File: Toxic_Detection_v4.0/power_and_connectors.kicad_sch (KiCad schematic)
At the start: 50 parts, among them IC7 ESDA6V1U1RL, IC8 AP7365-33WG-7, IC9 TPS2054BDR, J10 USB_C_Receptacle, J11 DM3AT-SF-PEJM5, J12 Conn_01x04_Pin, J13 Conn_ARM_JTAG_SWD_20, J8 Conn_01x04_Pin, J9 Conn_01x04_Pin

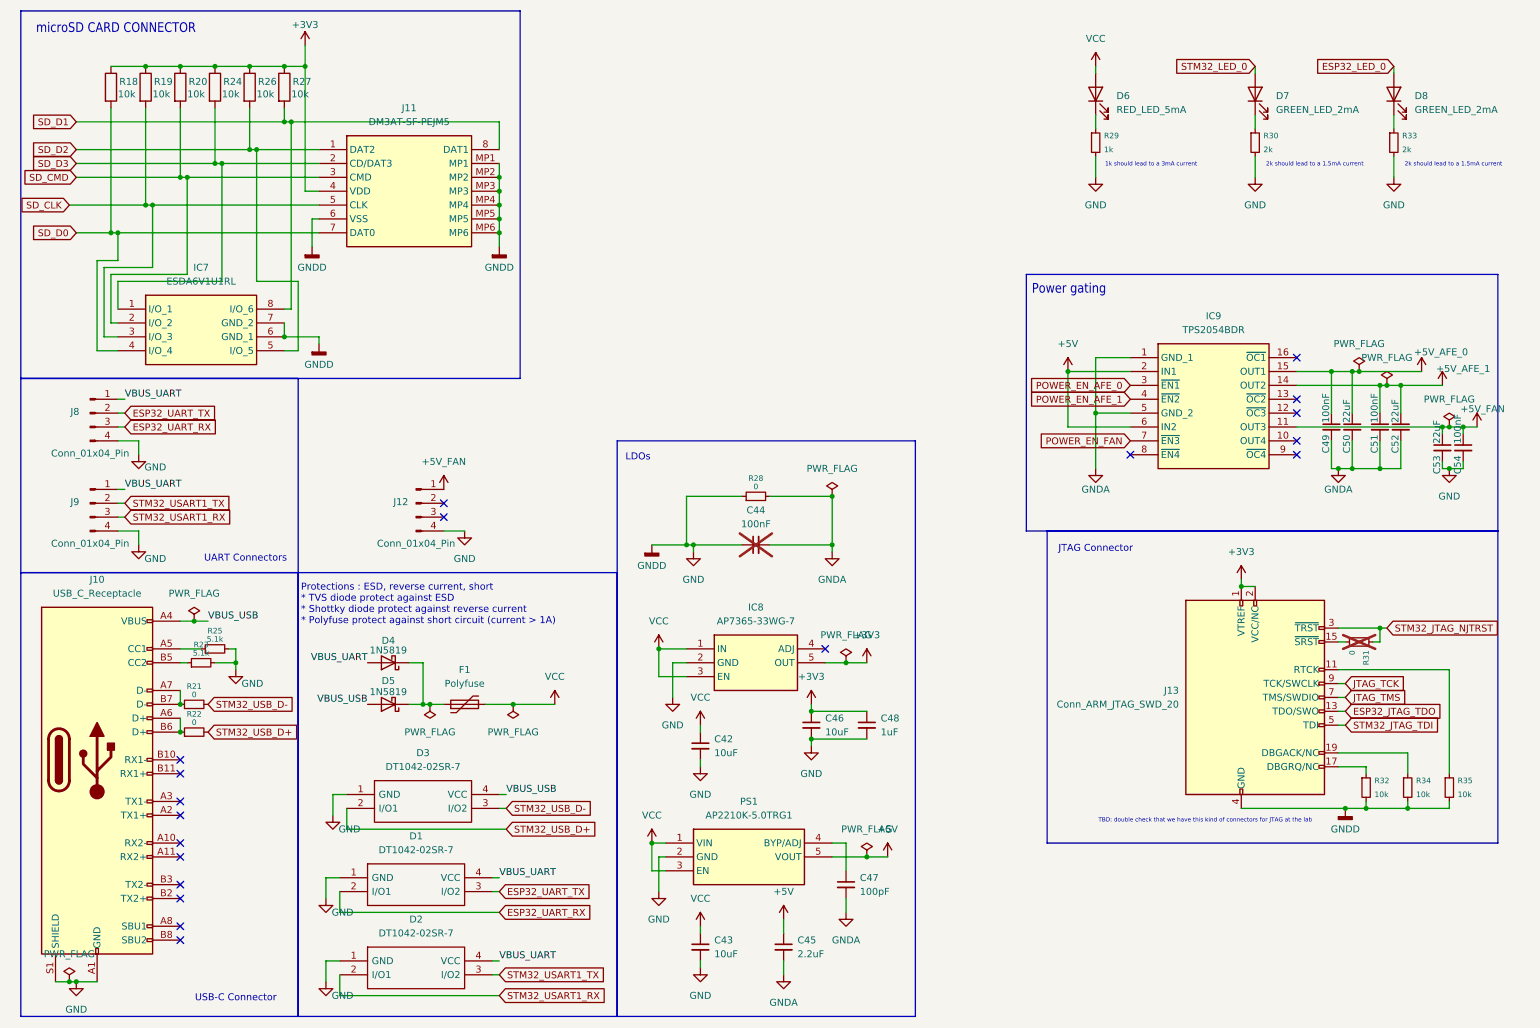
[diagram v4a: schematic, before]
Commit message: doc: update schematic documentation, design notes and all other kind of documentation. Add product_brief revision history
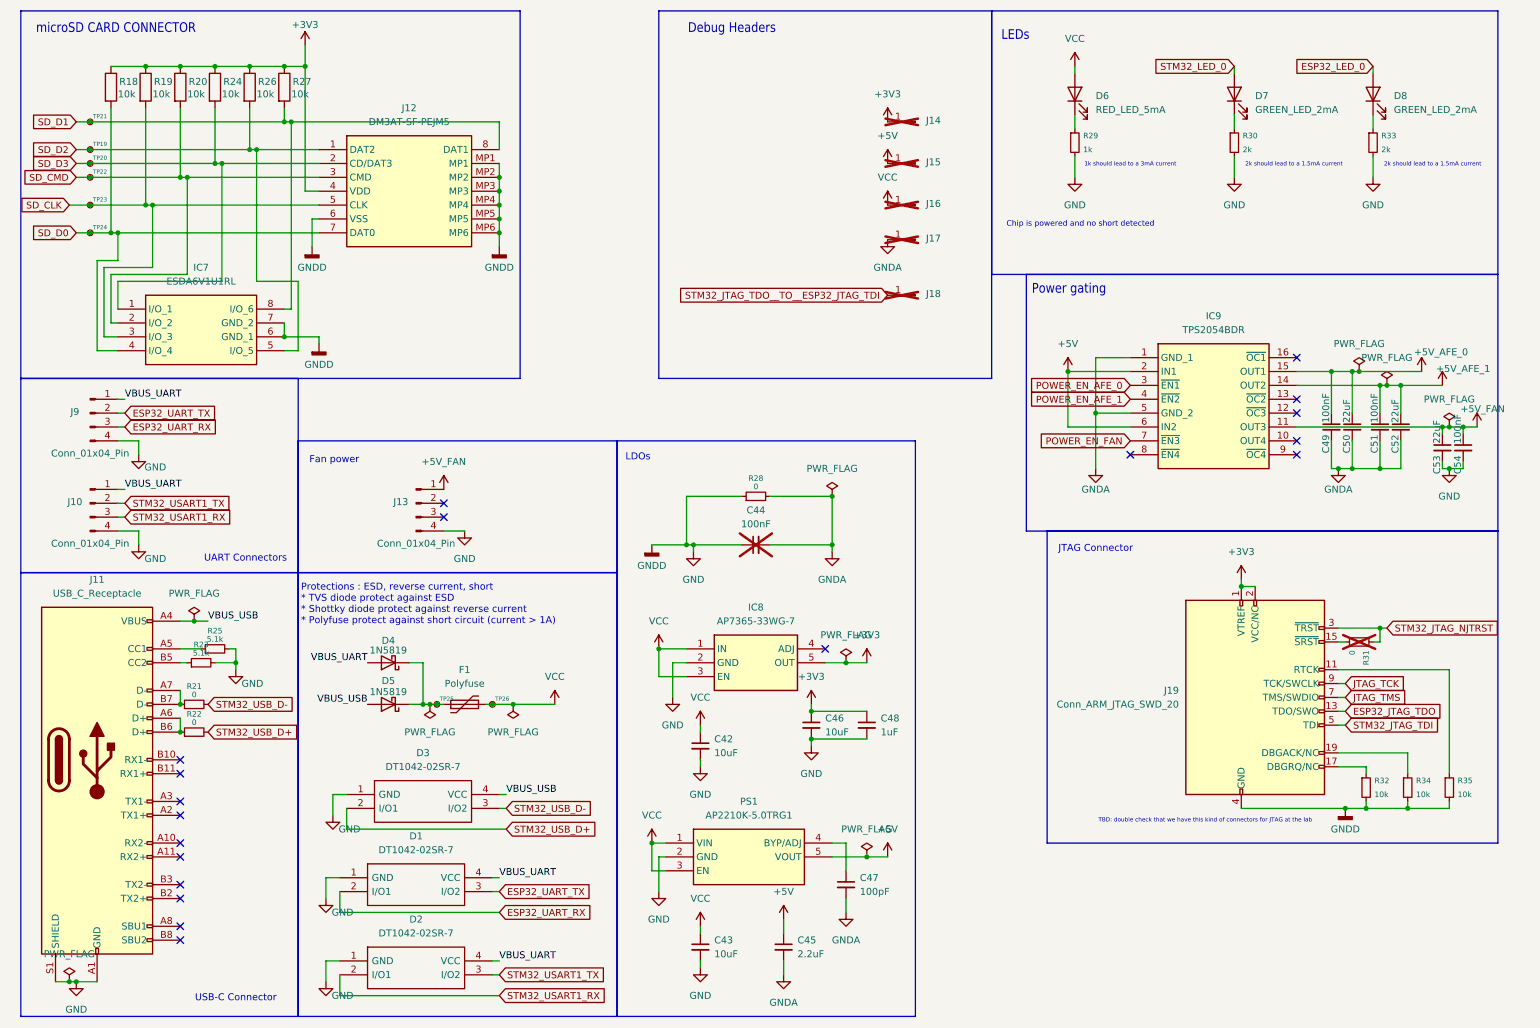
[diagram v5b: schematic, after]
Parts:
- added J14, J15, J16, J17, J18: Conn_01x01_Pin, Connector_PinSocket_2.54mm:PinSocket_1x01_P2.54mm_Vertical, symbol Connector:Conn_01x01_Pin
- added TP19, TP20, TP21, TP22, TP23, TP24, TP25, TP26: TestPoint_Small, TestPoint:TestPoint_Pad_D1.0mm, symbol Connector:TestPoint_Small
- renumbered J9 to J10, J10 to J11, J11 to J12, J12 to J13, J13 to J19, J8 to J9
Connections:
- net +3V3: now also J14.1 (Pin_1)
- net +5V: now also J15.1 (Pin_1)
- net GNDA: now also J17.1 (Pin_1)
- net SD_CLK: now also TP23.1
- net SD_CMD: now also TP22.1
- net SD_D0: now also TP24.1
- net SD_D1: now also TP21.1
- net SD_D2: now also TP19.1
- net SD_D3: now also TP20.1
- net VCC: now also J16.1 (Pin_1), TP26.1
- net at D4.1 (K), D5.1 (K), F1.1: now also TP25.1
- new net STM32_JTAG_TDO__TO__ESP32_JTAG_TDI: J18.1 (Pin_1)
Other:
- note added: "Chip is powered and no short detected"
- note added: "Debug Headers"
- note added: "Fan power"
- note added: "LEDs"
- company: (none) -> Company: LNIS
- title: (none) -> Toxic_Detection_PCB
- moved on the sheet: D6, D7, D8, R29, R30, R33

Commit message: feat: first placement (layout)
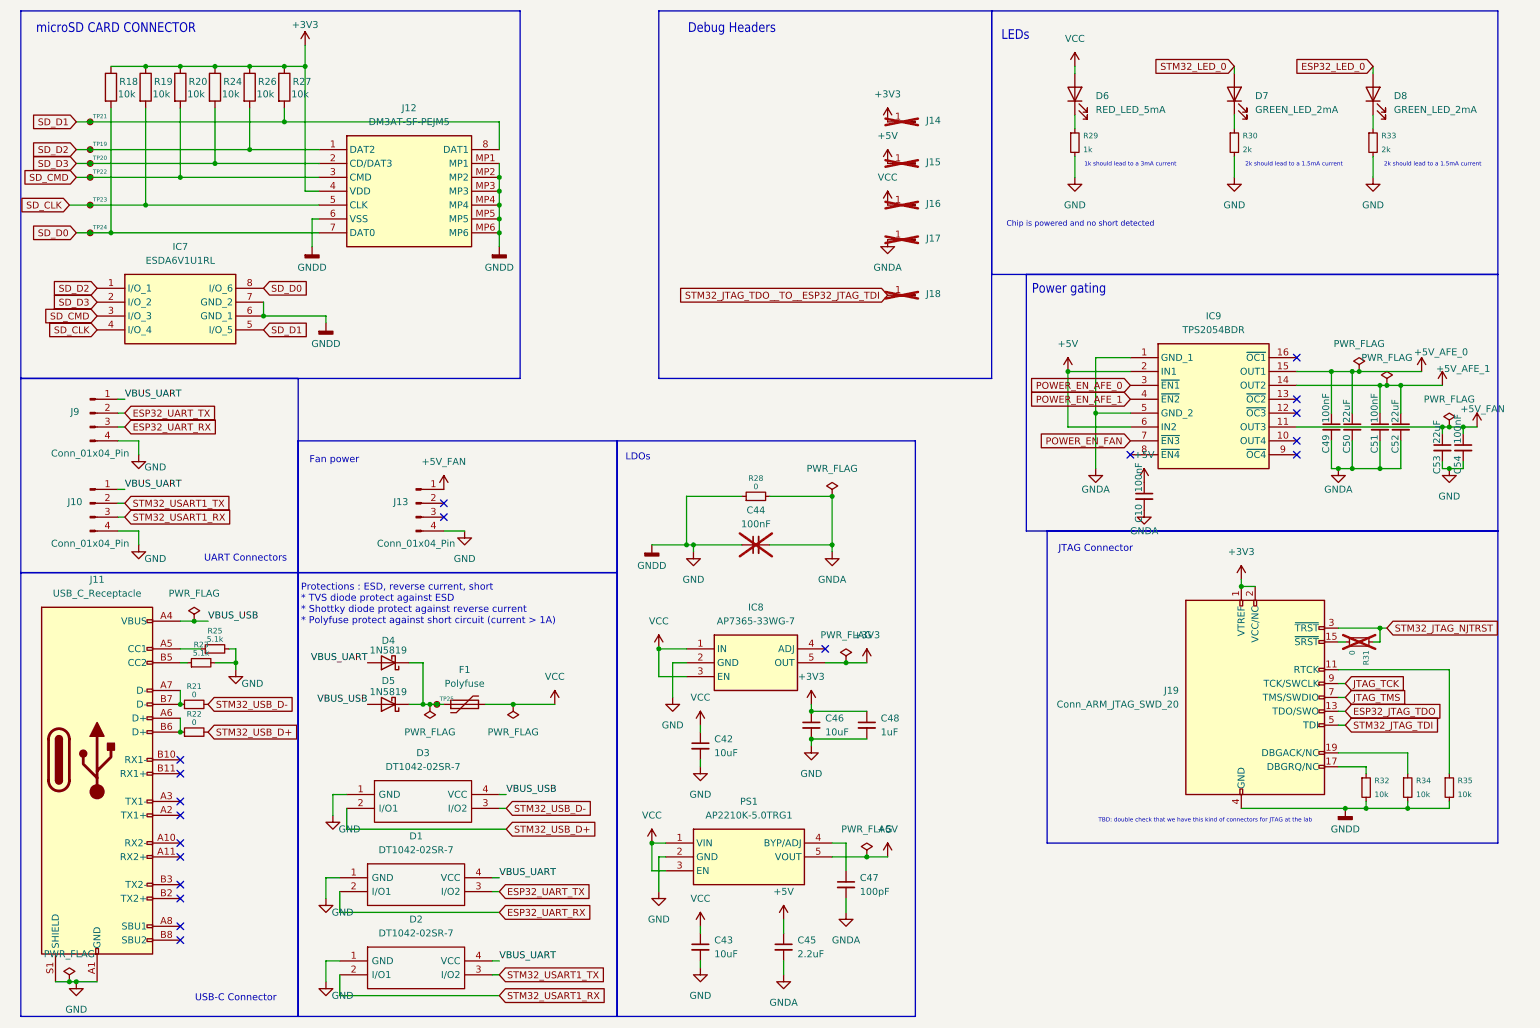
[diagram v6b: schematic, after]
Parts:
- removed TP26: TestPoint_Small, TestPoint:TestPoint_Pad_D1.0mm, symbol Connector:TestPoint_Small
- added C10: 100nF, Capacitor_SMD:C_0805_2012Metric_Pad1.18x1.45mm_HandSolder, symbol Device:C_Small
- J13: footprint Connector_PinSocket_2.54mm:PinSocket_1x04_P2.54mm_Vertical -> Connector_PinHeader_2.54mm:PinHeader_1x04_P2.54mm_Vertical
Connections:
- net +5V: now also C10.1
- net GNDA: now also C10.2
- net SD_CLK: now also IC7.4 (I/O_4); no longer IC7.3 (I/O_3)
- net SD_CMD: now also IC7.3 (I/O_3); no longer IC7.2 (I/O_2)
- net SD_D0: now also IC7.8 (I/O_6); no longer IC7.4 (I/O_4)
- net SD_D1: now also IC7.5 (I/O_5); no longer IC7.8 (I/O_6)
- net SD_D2: now also IC7.1 (I/O_1); no longer IC7.5 (I/O_5)
- net SD_D3: now also IC7.2 (I/O_2); no longer IC7.1 (I/O_1)
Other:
- moved on the sheet: IC7

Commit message: feat (layout) : finish routing, fill zones, and create custom footprints for some components
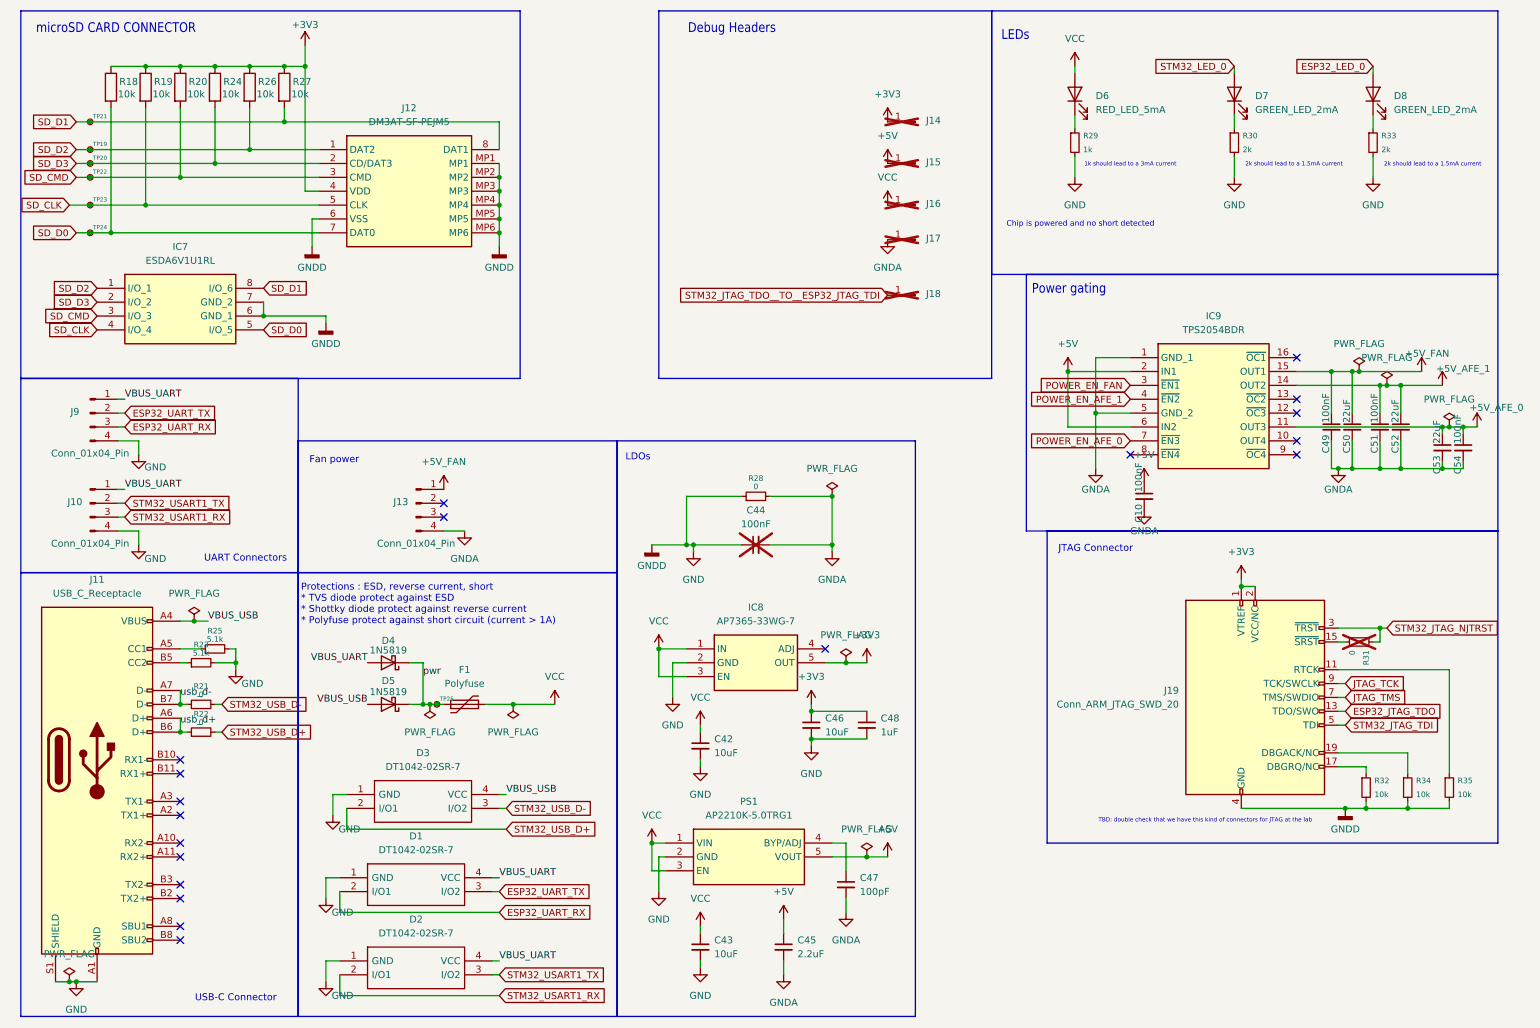
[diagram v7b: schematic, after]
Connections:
- net +5V_AFE_0: now also C53.1, C54.1, IC9.11 (OUT3); no longer C49.1, C50.1, IC9.15 (OUT1)
- net +5V_FAN: now also C49.1, C50.1, IC9.15 (OUT1); no longer C53.1, C54.1, IC9.11 (OUT3)
- net GND: no longer C53.2, C54.2, J13.4 (Pin_4)
- net GNDA: now also C53.2, C54.2, J13.4 (Pin_4)
- net POWER_EN_AFE_0: now also IC9.7 (~{EN3}); no longer IC9.3 (~{EN1})
- net POWER_EN_FAN: now also IC9.3 (~{EN1}); no longer IC9.7 (~{EN3})
- net SD_D0: now also IC7.5 (I/O_5); no longer IC7.8 (I/O_6)
- net SD_D1: now also IC7.8 (I/O_6); no longer IC7.5 (I/O_5)
- net pwr: now reaches D4.1 (K), D5.1 (K), F1.1, TP25.1
- net usb_d-: now reaches J11.A7 (D-), J11.B7 (D-), R21.1
- net usb_d+: now reaches J11.A6 (D+), J11.B6 (D+), R22.1
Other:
- moved on the sheet: R21, R22

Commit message: feat: take into account PE's feedback : update jtag connector, add second port for 2wires-fan, add pwm pin to control fan.
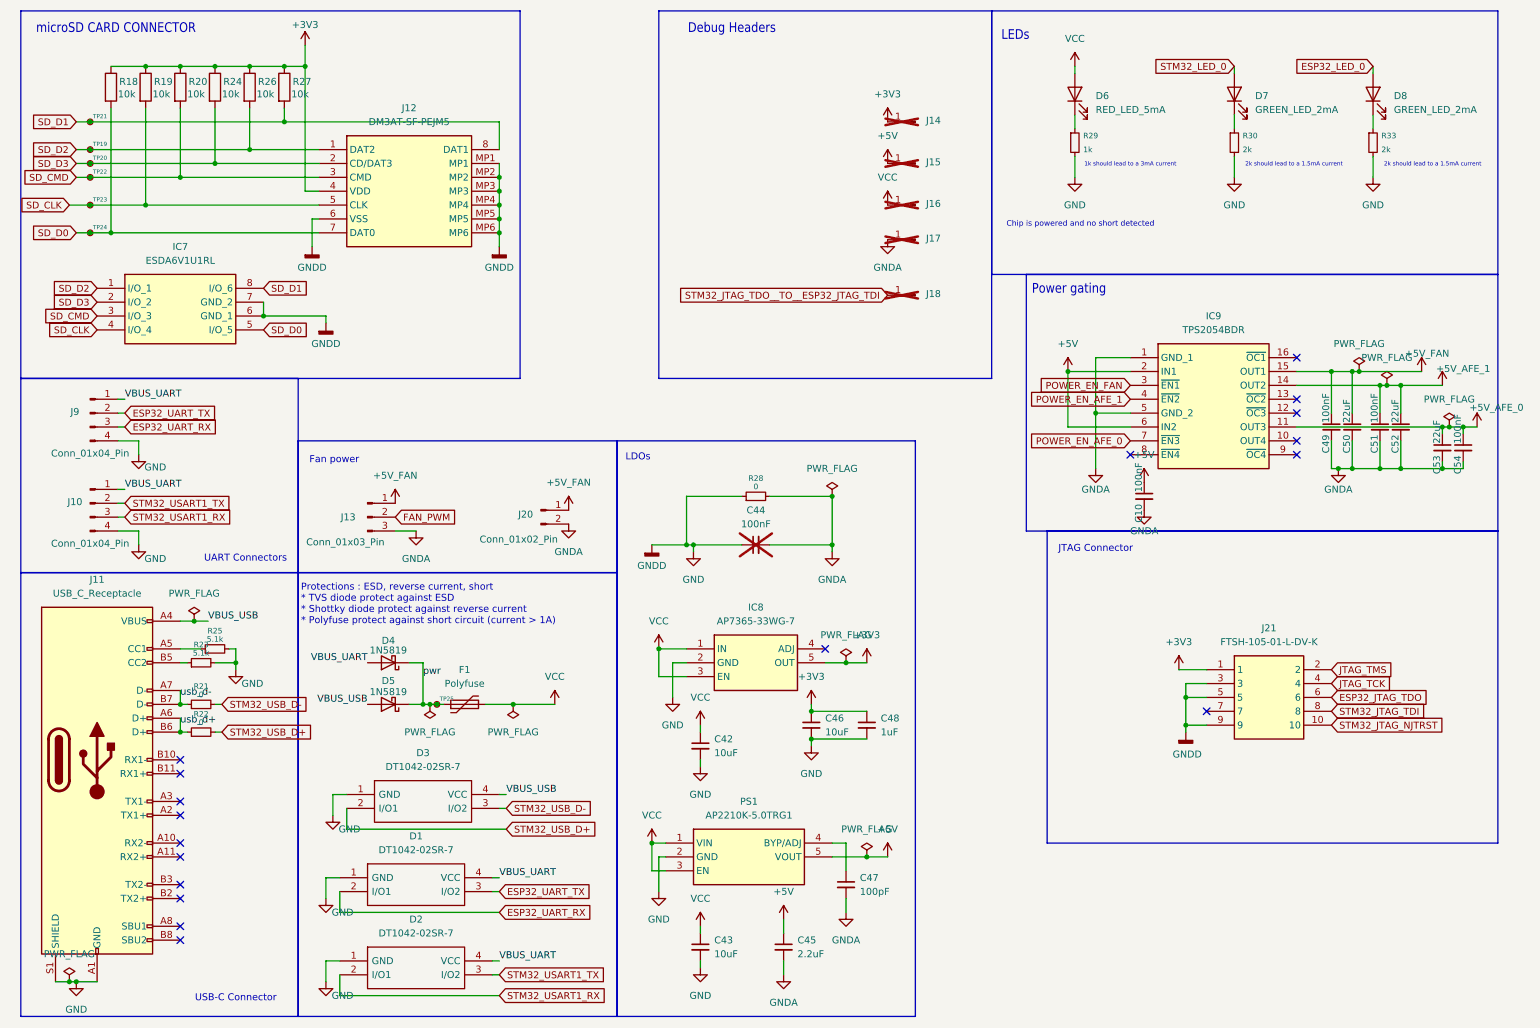
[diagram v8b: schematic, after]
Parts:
- removed J13: Conn_01x04_Pin, Connector_PinHeader_2.54mm:PinHeader_1x04_P2.54mm_Vertical, symbol Connector:Conn_01x04_Pin
- removed J19: Conn_ARM_JTAG_SWD_20, Connector_PinSocket_2.54mm:PinSocket_2x10_P2.54mm_Vertical, symbol Connector:Conn_ARM_JTAG_SWD_20
- removed R31: 0, Resistor_SMD:R_0805_2012Metric_Pad1.20x1.40mm_HandSolder, symbol Device:R_Small
- removed R32, R34, R35: 10k, Resistor_SMD:R_0805_2012Metric_Pad1.20x1.40mm_HandSolder, symbol Device:R_Small
- added J13: Conn_01x03_Pin, Connector_PinHeader_2.54mm:PinHeader_1x03_P2.54mm_Vertical, symbol Connector:Conn_01x03_Pin
- added J20: Conn_01x02_Pin, Connector_PinHeader_2.54mm:PinHeader_1x02_P2.54mm_Vertical, symbol Connector:Conn_01x02_Pin
- added J21: FTSH-105-01-L-DV-K, jtag connector:FTSH10501LDVK, symbol FTSH-105-01-L-DV-K:FTSH-105-01-L-DV-K
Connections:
- net +3V3: now also J21.1
- net +5V_FAN: now also J13.1 (Pin_1), J20.1 (Pin_1)
- net ESP32_JTAG_TDO: now also J21.6
- net GND: now also J21.3, J21.5, J21.9
- net GNDA: now also J13.3 (Pin_3), J20.2 (Pin_2)
- net JTAG_TCK: now also J21.4
- net JTAG_TMS: now also J21.2
- net STM32_JTAG_NJTRST: now also J21.10
- net STM32_JTAG_TDI: now also J21.8
- new net FAN_PWM: J13.2 (Pin_2)
- no-connect marks 19 -> 18
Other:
- note removed: "TBD: double check that we have this kind of connectors for JTAG at the lab"
